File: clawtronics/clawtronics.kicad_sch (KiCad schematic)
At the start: 23 parts, among them J1 TYPE-C-31-M-12, J2 Conn_01x20_Pin, J3 Conn_01x20_Pin, J4 Screw_Terminal_01x02, SW1 TS-1088-AR02016, SW2 TS-1088-AR02016, U2 ESP32-S3-WROOM-1, U3 LD1117S33TR_SOT223, U4 TDN_5-2412WISM

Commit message: pcb progress
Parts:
- removed J4: Screw_Terminal_01x02, symbol Connector:Screw_Terminal_01x02
- removed U4: TDN_5-2412WISM, Converter_DCDC:Converter_DCDC_TRACO_TDN_5-xxxxWISM_SMD, symbol Regulator_Switching:TDN_5-2412WISM
- added J4: Power, Connector_Phoenix_MSTB:PhoenixContact_MSTBV_2,5_6-GF-5,08_1x06_P5.08mm_Vertical_ThreadedFlange_MountHole, symbol Connector:Screw_Terminal_01x06
- renumbered C4 to C1, C1 to C2, C2 to C3, C3 to C4, R2 to R1, R1 to R2, R4 to R3, R5 to R4, R6 to R5, R3 to R6, SW2 to SW1, SW1 to SW2, U2 to U1, U3 to U2
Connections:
- net +12V: now also J4.3 (Pin_3)
- net +5V: now also J4.5 (Pin_5)
- net GND: now also J4.2 (Pin_2), J4.4 (Pin_4), J4.6 (Pin_6)
- new net +24V: J4.1 (Pin_1)
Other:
- note removed: "24V in"

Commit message: figured out switches
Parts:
- J4: footprint Connector_Phoenix_MSTB:PhoenixContact_MSTBV_2,5_6-GF-5,08_1x06_P5.08mm_Vertical_ThreadedFlange_MountHole -> TerminalBlock_MetzConnect:TerminalBlock_MetzConnect_Type011_RT05506HBLC_1x06_P5.00mm_Horizontal
- SW1, SW2: footprint easyeda2kicad:SW-SMD_L3.9-W3.0-P4.45 -> Button_Switch_SMD:SW_SPST_TS-1088-xR020

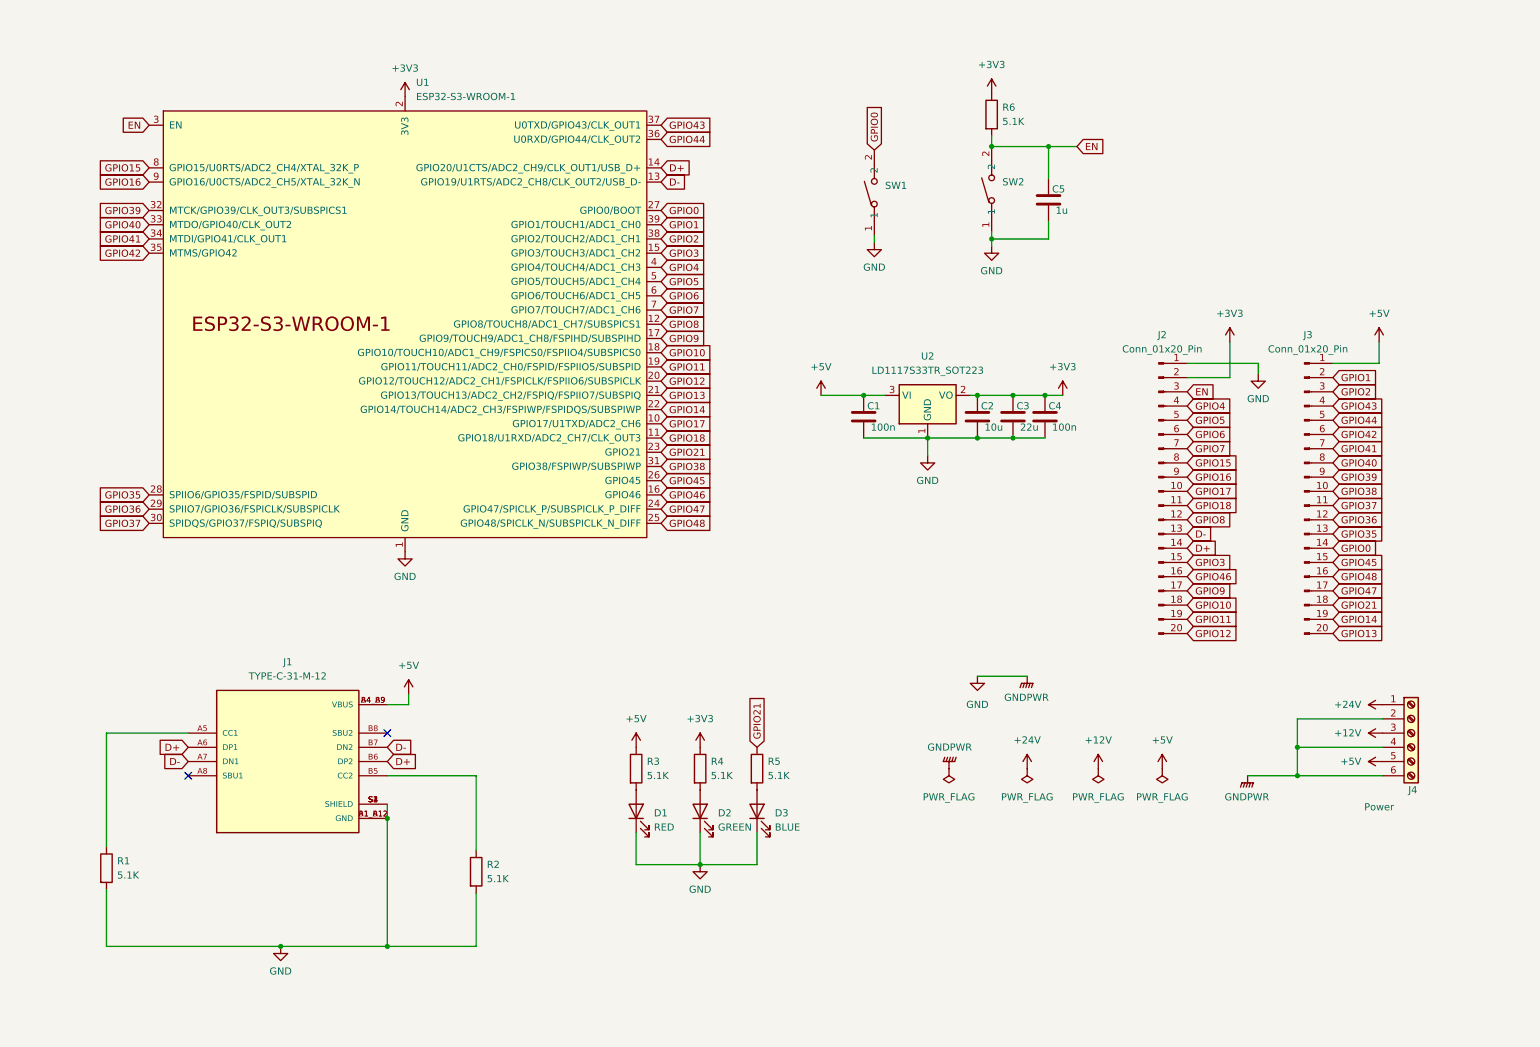
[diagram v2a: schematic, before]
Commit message: layout with hierarchical sheets
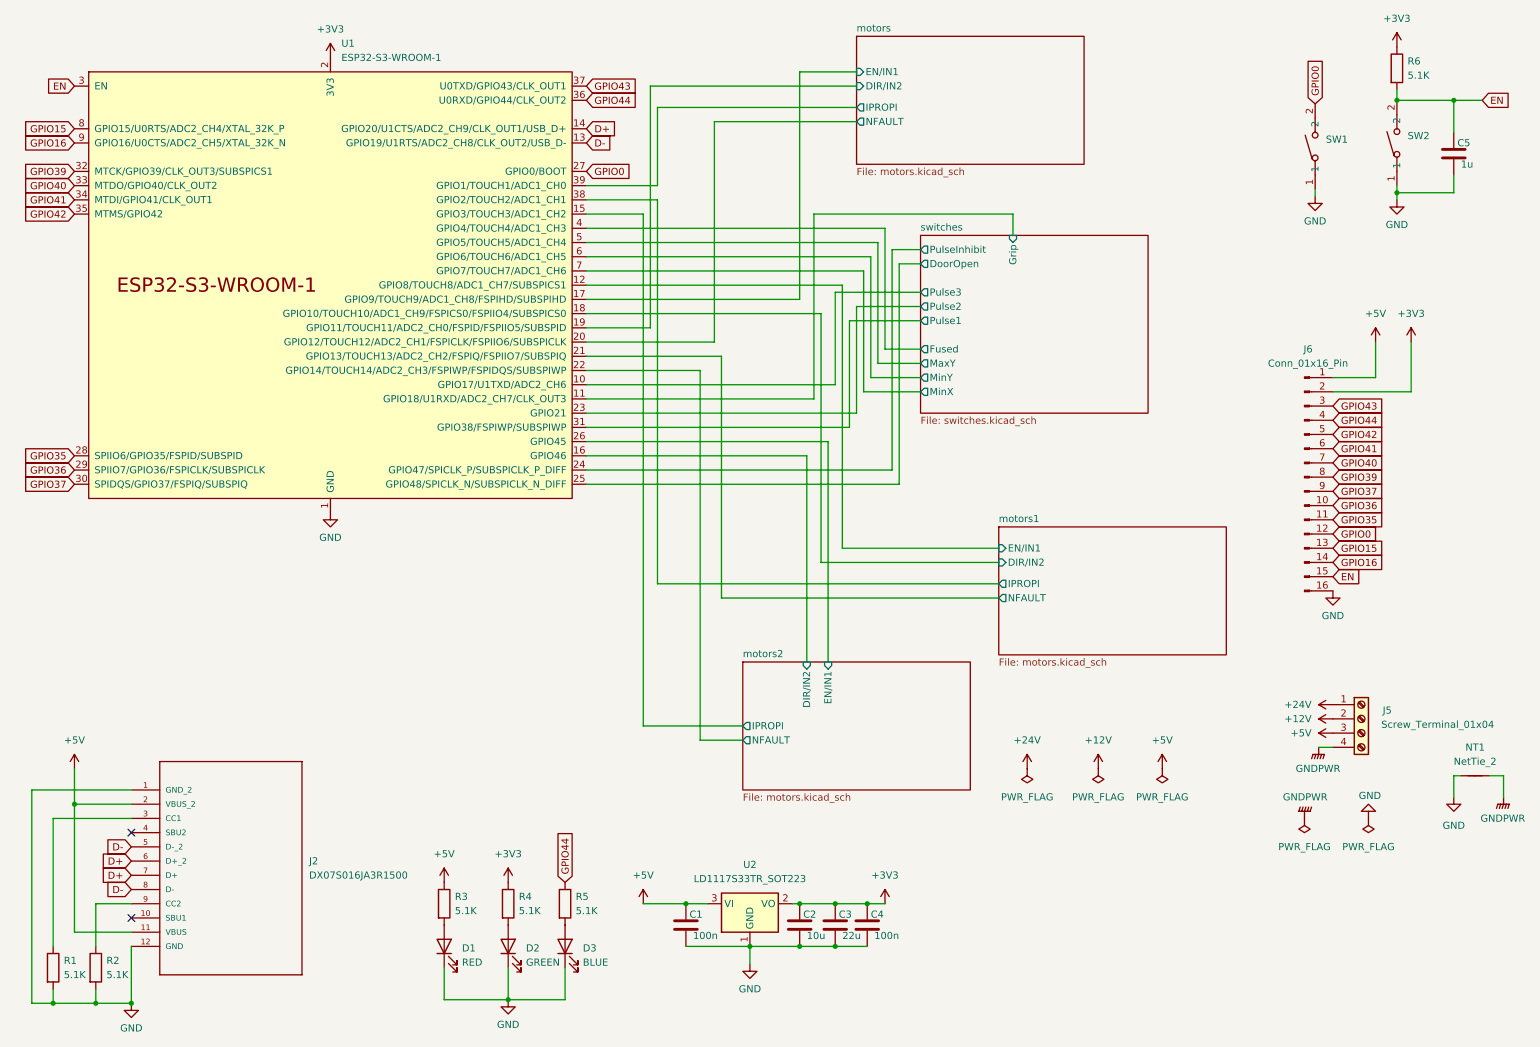
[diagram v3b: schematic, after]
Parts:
- removed J1: TYPE-C-31-M-12, TYPE-C-31-M-12:HRO_TYPE-C-31-M-12, symbol TYPE-C-31-M-12:TYPE-C-31-M-12
- removed J2, J3: Conn_01x20_Pin, Connector_PinHeader_2.54mm:PinHeader_1x20_P2.54mm_Vertical, symbol Connector:Conn_01x20_Pin
- removed J4: Power, TerminalBlock_MetzConnect:TerminalBlock_MetzConnect_Type011_RT05506HBLC_1x06_P5.00mm_Horizontal, symbol Connector:Screw_Terminal_01x06
- added J2: DX07S016JA3R1500, clawtronics:CONN12_DX07S_JAE, symbol New_Library:DX07S016JA3R1500
- added J5: Screw_Terminal_01x04, TerminalBlock_Phoenix:TerminalBlock_Phoenix_MKDS-1,5-4_1x04_P5.00mm_Horizontal, symbol Connector:Screw_Terminal_01x04
- added J6: Conn_01x16_Pin, Connector_PinHeader_1.00mm:PinHeader_1x16_P1.00mm_Vertical, symbol Connector:Conn_01x16_Pin
- added NT1: NetTie_2, symbol Device:NetTie_2
- SW1, SW2: value TS-1088-AR02016 -> SW_SPST_TS-1088-xR020; LCSC Part C720477 -> (none); MF XUNPU -> (none); MP TS-1088-AR02016 -> (none)
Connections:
- net +12V: now also J5.2 (Pin_2)
- net +24V: now also J5.1 (Pin_1)
- net +3V3: now also J6.2 (Pin_2)
- net +5V: now also J2.11 (VBUS), J2.2 (VBUS_2), J5.3 (Pin_3), J6.1 (Pin_1)
- net D+: now also J2.6 (D+_2), J2.7 (D+)
- net D-: now also J2.5 (D-_2), J2.8 (D-)
- net EN: now also J6.15 (Pin_15)
- net GND: now also J2.1 (GND_2), J2.12 (GND), J6.16 (Pin_16), NT1.1
- net GPIO0: now also J6.12 (Pin_12)
- net GPIO15: now also J6.13 (Pin_13)
- net GPIO16: now also J6.14 (Pin_14)
- net GPIO35: now also J6.11 (Pin_11)
- net GPIO36: now also J6.10 (Pin_10)
- net GPIO37: now also J6.9 (Pin_9)
- net GPIO39: now also J6.8 (Pin_8)
- net GPIO40: now also J6.7 (Pin_7)
- net GPIO41: now also J6.6 (Pin_6)
- net GPIO42: now also J6.5 (Pin_5)
- net GPIO43: now also J6.3 (Pin_3)
- net GPIO44: now also R5.1, J6.4 (Pin_4)
- net at R2.1: now also J2.9 (CC2)
- net at R1.1: now also J2.3 (CC1)
- net GPIO1 renamed motors/IPROPI
- net GPIO10 renamed motors1/DIR/IN2
- net GPIO11 renamed motors/DIR/IN2
- net GPIO12 renamed motors/NFAULT
- net GPIO13 renamed motors1/NFAULT
- net GPIO14 renamed motors2/NFAULT
- net GPIO17 renamed switches/Pulse3
- net GPIO18 renamed switches/Grip
- net GPIO2 renamed motors1/IPROPI
- net GPIO21 renamed switches/Pulse2
- net switches/Pulse2: no longer R5.1
- net GPIO3 renamed motors2/IPROPI
- net GPIO38 renamed switches/Pulse1
- net GPIO4 renamed switches/Fused
- net GPIO45 renamed motors2/EN/IN1
- net GPIO46 renamed motors2/DIR/IN2
- net GPIO47 renamed switches/PulseInhibit
- net GPIO48 renamed switches/DoorOpen
- net GPIO5 renamed switches/MaxY
- net GPIO6 renamed switches/MinY
- net GPIO7 renamed switches/MinX
- net GPIO8 renamed motors1/EN/IN1
- net GPIO9 renamed motors/EN/IN1
- new net GNDPWR: J5.4 (Pin_4), NT1.2
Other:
- added sheet motors (motors.kicad_sch)
- added sheet motors1 (motors.kicad_sch)
- added sheet motors2 (motors.kicad_sch)
- added sheet switches (switches.kicad_sch)
- moved on the sheet: C1, C2, C3, C4, C5, D1, D2, D3, R1, R3, R4, R5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

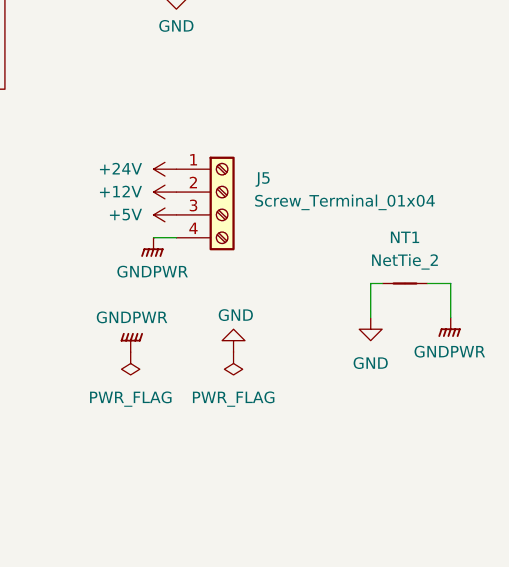
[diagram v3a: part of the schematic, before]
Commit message: update BOM with PNs
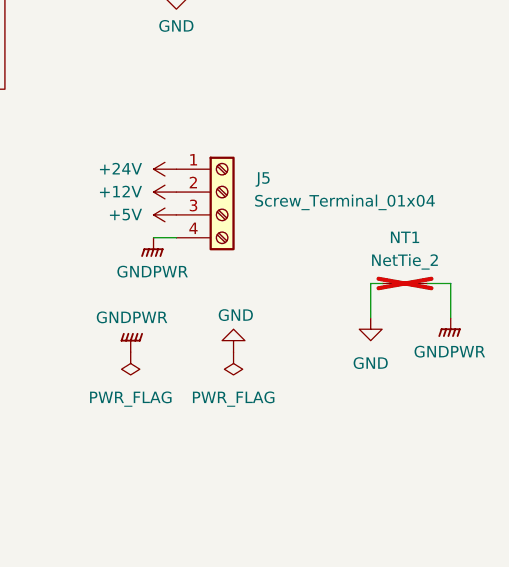
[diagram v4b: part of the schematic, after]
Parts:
- C1, C4: Part Number (none) -> C0603C104J3RACTU
- C2: Part Number (none) -> 0603W106M6R3XD
- C3: Part Number (none) -> 0603W226M100BD
- C5: Part Number (none) -> 0603B105K100XD
- D1: Part Number (none) -> SML-D12U8WT86
- D2: Part Number (none) -> SML-D13M8WT86
- D3: Part Number (none) -> SMLEN3BC8TT86
- J2: Part Number (none) -> DX07S016JA3R1500
- J5: Part Number (none) -> 1869088
- J6: Part Number (none) -> SM16B-SHLS-TF(LF)(SN)
- NT1: now not fitted
- R1, R2, R3, R4, R5, R6: Part Number (none) -> RC0603FR-105K1L
- SW1, SW2: Part Number (none) -> GPTS203211B
- U1: Part Number (none) -> ESP32-S3-WROOM-1U-N8R8
- U2: Part Number (none) -> LD1117S33TR

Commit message: update footprints
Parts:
- C1, C4: value 100n -> 0.1u
- SW1, SW2: Part Number GPTS203211B -> B3U-1000P
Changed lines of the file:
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@@
 			)
 		)
-		(property "Value" "100n"
+		(property "Value" "0.1u"
 			(at 167.005 179.705 0)
 			(show_name no)
@@
 			)
 		)
-		(property "Datasheet" ""
+		(property "Datasheet" "https://www.digikey.com/en/products/detail/omron-electronics-inc-emc-div/B3U-1000P/1534338"
 			(at 270.51 38.1 0)
 			(hide yes)
@@
 			)
 		)
-		(property "Part Number" "GPTS203211B"
+		(property "Part Number" "B3U-1000P"
 			(at 260.35 38.1 90)
 			(hide yes)
@@
 			)
 		)
-		(property "Datasheet" ""
+		(property "Datasheet" "https://www.digikey.com/en/products/detail/omron-electronics-inc-emc-div/B3U-1000P/1534338"
 			(at 255.905 38.735 0)
 			(hide yes)
@@
 			)
 		)
-		(property "Part Number" "GPTS203211B"
+		(property "Part Number" "B3U-1000P"
 			(at 245.745 38.735 90)
 			(hide yes)
@@
 			)
 		)
-		(property "Value" "100n"
+		(property "Value" "0.1u"
 			(at 134.62 179.705 0)
 			(show_name no)
